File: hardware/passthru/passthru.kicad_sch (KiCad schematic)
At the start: 81 parts, among them J1 ARM_SWD, J2 RJ45_LED_Shielded, J3 Screw_Terminal_01x02, Q1 Q_PMOS_DGS, Q2 Q_PMOS_DGS, Q3 Q_NPN_BEC, U1 EFM32GG11B8xx, U2 KSZ8081RND, U3 LM5085, U4 TPS2375-1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

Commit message: passthru: change package for C28
This is a larger-capacity capacitor.
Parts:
- C28: footprint Capacitor_SMD:C_0603_1608Metric_Pad1.08x0.95mm_HandSolder -> Capacitor_SMD:CP_Elec_6.3x5.8
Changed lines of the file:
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@@
       (effects (font (size 1.27 1.27)) (justify left))
     )
-    (property "Footprint" "Capacitor_SMD:C_0603_1608Metric_Pad1.08x0.95mm_HandSolder" (id 2) (at 260.35 152.4 0)
+    (property "Footprint" "Capacitor_SMD:CP_Elec_6.3x5.8" (id 2) (at 260.35 152.4 0)
       (effects (font (size 1.27 1.27)) hide)
     )
@@
     )
     (path "/3e114920-c983-47e2-a4af-ffa9d93bf066"
-      (reference "C28") (unit 1) (value "100u") (footprint "Capacitor_SMD:C_0603_1608Metric_Pad1.08x0.95mm_HandSolder")
+      (reference "C28") (unit 1) (value "100u") (footprint "Capacitor_SMD:CP_Elec_6.3x5.8")
     )
     (path "/705e5d5e-846d-457e-8c79-943d88941cdd"

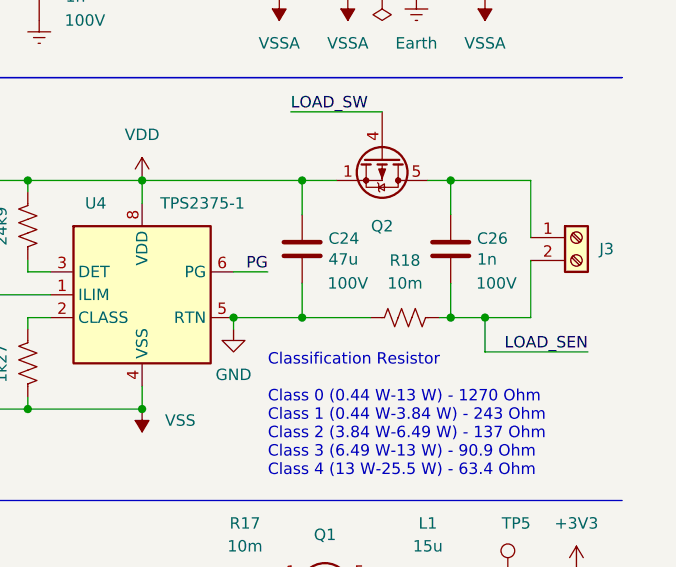
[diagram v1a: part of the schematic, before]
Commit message: passthru: increase the resistance of the VDD shunt resistor
Assuming a maximum VDD current of 600 mA, this will give a maximum
sense voltage of 0.6 V and 36 mW of power draw.
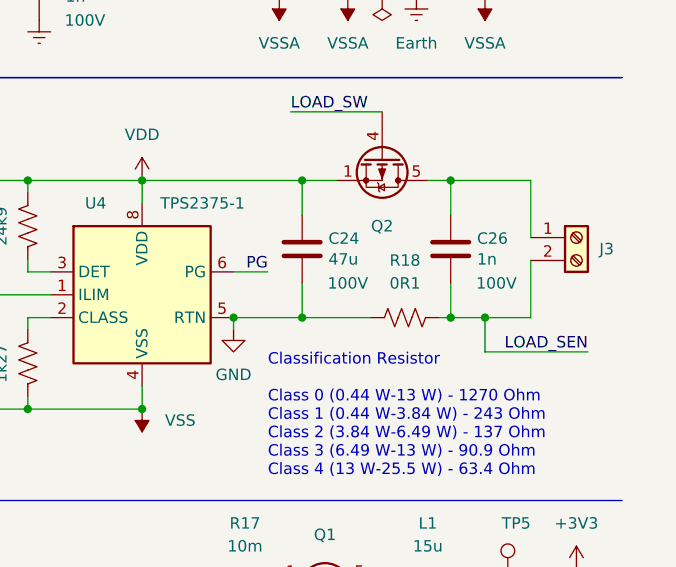
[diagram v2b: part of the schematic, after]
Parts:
- R18: value 10m -> 0R1
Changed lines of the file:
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@@
     (in_bom yes) (on_board yes) (fields_autoplaced)
     (property "Reference" "R18" (id 0) (at 241.3 104.14 90))
-    (property "Value" "10m" (id 1) (at 241.3 106.68 90))
+    (property "Value" "0R1" (id 1) (at 241.3 106.68 90))
     (property "Footprint" "Resistor_SMD:R_0805_2012Metric_Pad1.20x1.40mm_HandSolder" (id 2) (at 241.554 109.474 90)
       (effects (font (size 1.27 1.27)) hide)
@@
     )
     (path "/2fbf6397-d758-4da9-b1f6-76896aa5eb14"
-      (reference "R18") (unit 1) (value "10m") (footprint "Resistor_SMD:R_0805_2012Metric_Pad1.20x1.40mm_HandSolder")
+      (reference "R18") (unit 1) (value "0R1") (footprint "Resistor_SMD:R_0805_2012Metric_Pad1.20x1.40mm_HandSolder")
     )
     (path "/49b4fa8c-c9be-4919-acc5-cb23c2bb3e6c"

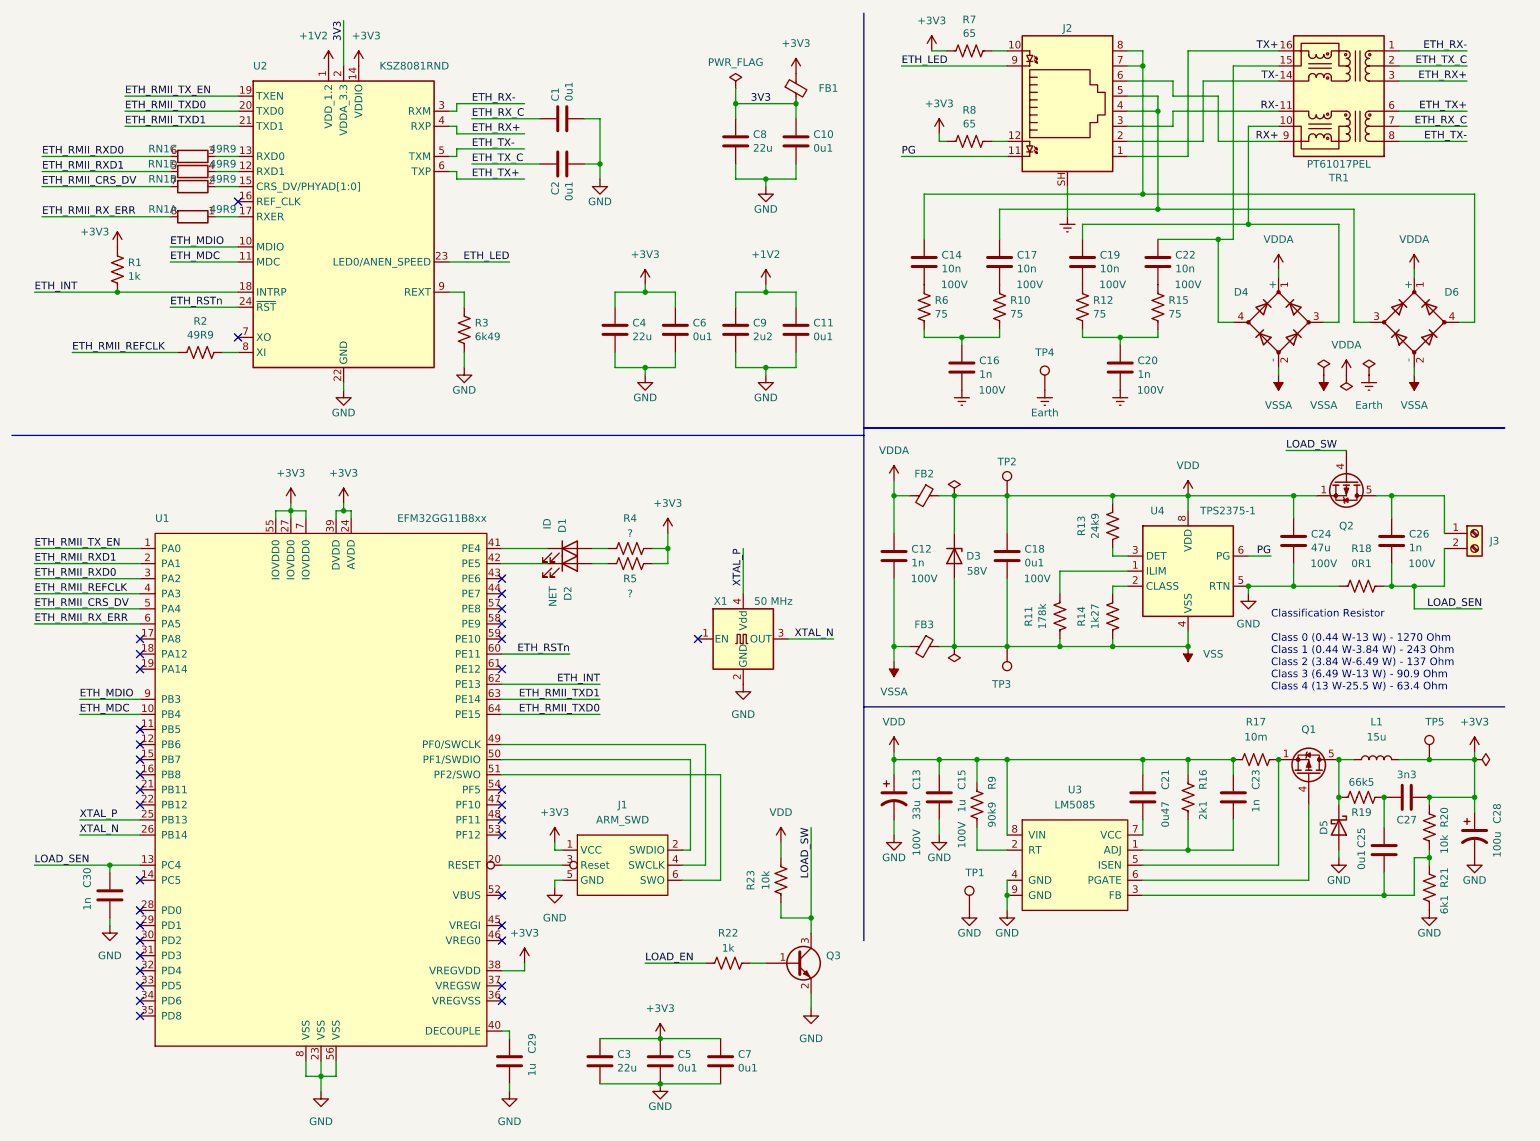
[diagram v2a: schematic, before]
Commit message: passthru: update resistor values
The 6.1 kΩ resistor was hard to find. I also added the
current-limiting resistors for the LEDs.
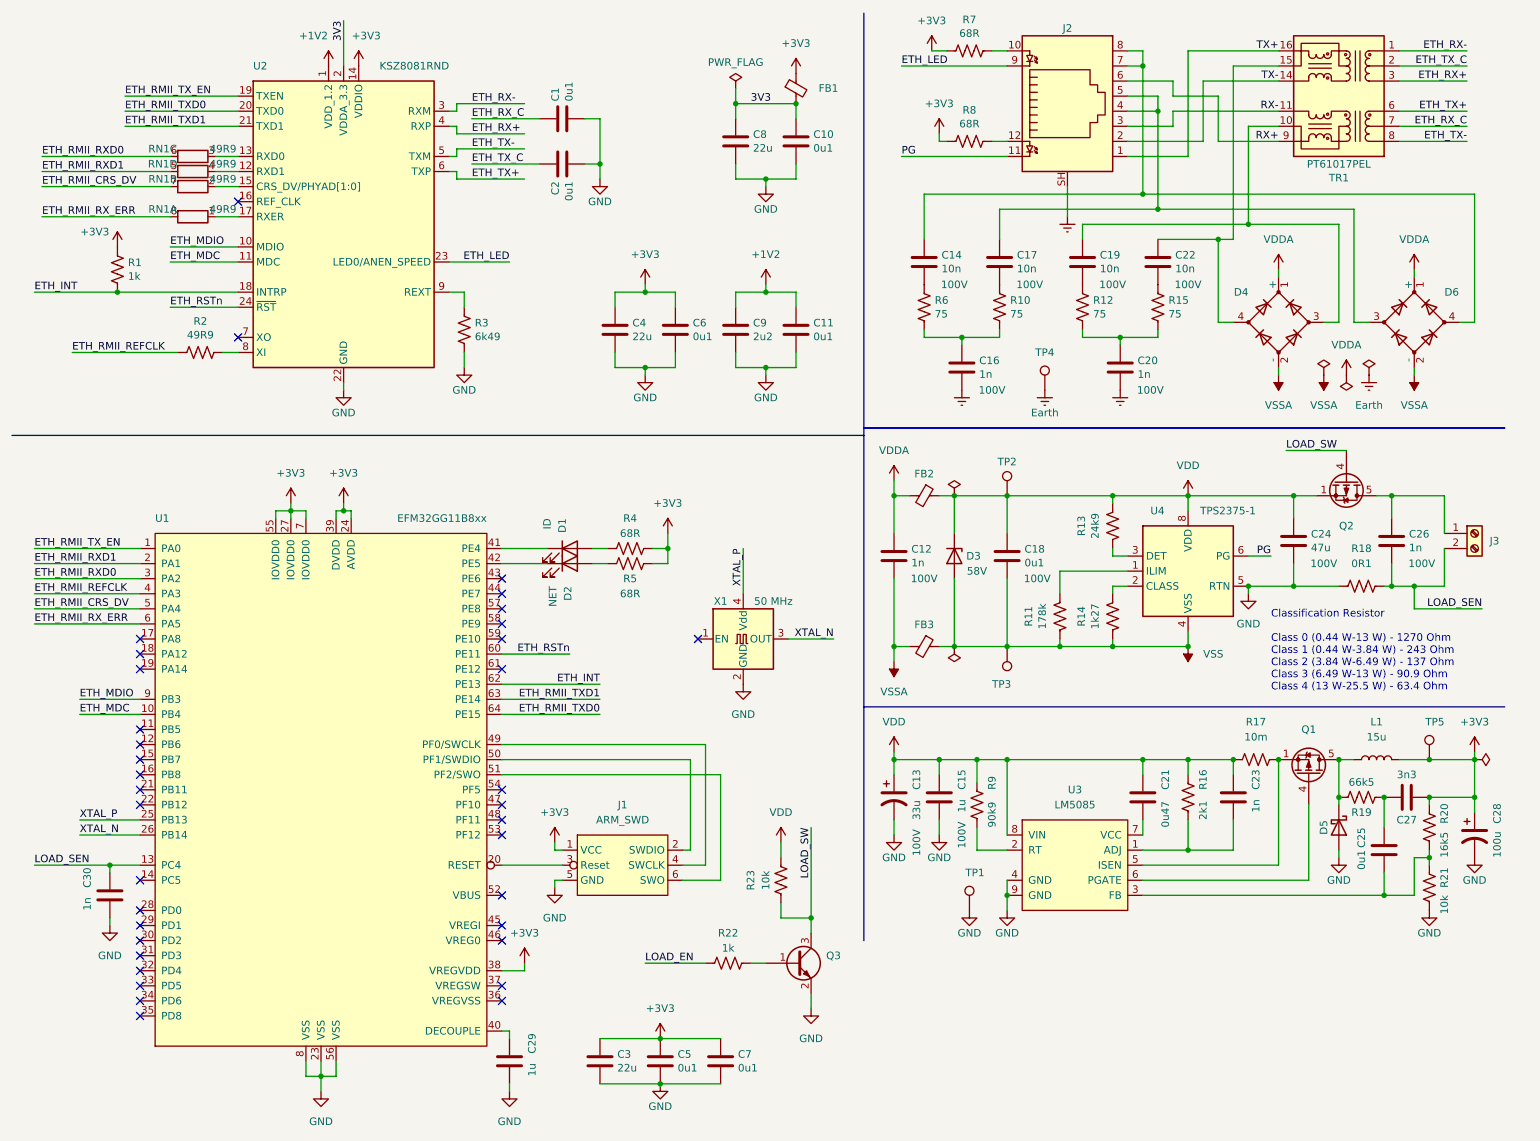
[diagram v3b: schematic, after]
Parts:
- R20: value 10k -> 16k5
- R21: value 6k1 -> 10k
- R4, R5: value ? -> 68R
- R7, R8: value 65 -> 68R; footprint Capacitor_SMD:C_0603_1608Metric_Pad1.08x0.95mm_HandSolder -> Resistor_SMD:R_0603_1608Metric_Pad0.98x0.95mm_HandSolder
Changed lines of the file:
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@@
   (symbol (lib_id "Device:R_US") (at 252.73 151.13 0) (unit 1)
     (in_bom yes) (on_board yes)
-    (property "Reference" "R20" (id 0) (at 255.27 151.13 90)
-      (effects (font (size 1.27 1.27)) (justify left))
-    )
-    (property "Value" "10k" (id 1) (at 255.27 155.575 90)
+    (property "Reference" "R20" (id 0) (at 255.27 150.495 90)
+      (effects (font (size 1.27 1.27)) (justify left))
+    )
+    (property "Value" "16k5" (id 1) (at 255.27 156.21 90)
       (effects (font (size 1.27 1.27)) (justify left))
     )
@@
     (in_bom yes) (on_board yes)
     (property "Reference" "R8" (id 0) (at 175.26 30.3022 90))
-    (property "Value" "65" (id 1) (at 175.26 32.6136 90))
-    (property "Footprint" "Capacitor_SMD:C_0603_1608Metric_Pad1.08x0.95mm_HandSolder" (id 2) (at 175.006 36.576 90)
+    (property "Value" "68R" (id 1) (at 175.26 32.6136 90))
+    (property "Footprint" "Resistor_SMD:R_0603_1608Metric_Pad0.98x0.95mm_HandSolder" (id 2) (at 175.006 36.576 90)
       (effects (font (size 1.27 1.27)) hide)
     )
@@
     (in_bom yes) (on_board yes)
     (property "Reference" "R7" (id 0) (at 175.26 15.0622 90))
-    (property "Value" "65" (id 1) (at 175.26 17.3736 90))
-    (property "Footprint" "Capacitor_SMD:C_0603_1608Metric_Pad1.08x0.95mm_HandSolder" (id 2) (at 175.006 21.336 90)
+    (property "Value" "68R" (id 1) (at 175.26 17.3736 90))
+    (property "Footprint" "Resistor_SMD:R_0603_1608Metric_Pad0.98x0.95mm_HandSolder" (id 2) (at 175.006 21.336 90)
       (effects (font (size 1.27 1.27)) hide)
     )
@@
     (in_bom yes) (on_board yes)
     (property "Reference" "R5" (id 0) (at 118.11 109.22 90))
-    (property "Value" "?" (id 1) (at 118.11 111.76 90))
+    (property "Value" "68R" (id 1) (at 118.11 111.76 90))
     (property "Footprint" "Resistor_SMD:R_0603_1608Metric_Pad0.98x0.95mm_HandSolder" (id 2) (at 118.364 105.664 90)
       (effects (font (size 1.27 1.27)) hide)
@@
     (in_bom yes) (on_board yes)
     (property "Reference" "R4" (id 0) (at 118.11 99.06 90))
-    (property "Value" "?" (id 1) (at 118.11 101.6 90))
+    (property "Value" "68R" (id 1) (at 118.11 101.6 90))
     (property "Footprint" "Resistor_SMD:R_0603_1608Metric_Pad0.98x0.95mm_HandSolder" (id 2) (at 118.364 103.124 90)
       (effects (font (size 1.27 1.27)) hide)
@@
       (effects (font (size 1.27 1.27)) (justify left))
     )
-    (property "Value" "6k1" (id 1) (at 255.27 165.735 90)
+    (property "Value" "10k" (id 1) (at 255.27 165.735 90)
       (effects (font (size 1.27 1.27)) (justify left))
     )
@@
     )
     (path "/a704724f-4b2e-47f2-9716-1986d43798c2"
-      (reference "R4") (unit 1) (value "?") (footprint "Resistor_SMD:R_0603_1608Metric_Pad0.98x0.95mm_HandSolder")
+      (reference "R4") (unit 1) (value "68R") (footprint "Resistor_SMD:R_0603_1608Metric_Pad0.98x0.95mm_HandSolder")
     )
     (path "/9d4e9158-a79b-4cd2-a875-493d31ceebff"
-      (reference "R5") (unit 1) (value "?") (footprint "Resistor_SMD:R_0603_1608Metric_Pad0.98x0.95mm_HandSolder")
+      (reference "R5") (unit 1) (value "68R") (footprint "Resistor_SMD:R_0603_1608Metric_Pad0.98x0.95mm_HandSolder")
     )
     (path "/2e130a9d-a852-4c24-b5aa-0bcd4d7d6efc"
@@
     )
     (path "/8215b5c3-e92a-447c-93b6-8f77bba9d70d"
-      (reference "R7") (unit 1) (value "65") (footprint "Capacitor_SMD:C_0603_1608Metric_Pad1.08x0.95mm_HandSolder")
+      (reference "R7") (unit 1) (value "68R") (footprint "Resistor_SMD:R_0603_1608Metric_Pad0.98x0.95mm_HandSolder")
     )
     (path "/7defcb95-dc82-483d-8346-733eed4831e7"
-      (reference "R8") (unit 1) (value "65") (footprint "Capacitor_SMD:C_0603_1608Metric_Pad1.08x0.95mm_HandSolder")
+      (reference "R8") (unit 1) (value "68R") (footprint "Resistor_SMD:R_0603_1608Metric_Pad0.98x0.95mm_HandSolder")
     )
     (path "/c54f8170-45ef-4d10-a60a-edfecf86c5a3"
@@
     )
     (path "/6a2fc3c1-7ad8-4e78-a7bf-386619f2ac37"
-      (reference "R20") (unit 1) (value "10k") (footprint "Resistor_SMD:R_0603_1608Metric_Pad0.98x0.95mm_HandSolder")
+      (reference "R20") (unit 1) (value "16k5") (footprint "Resistor_SMD:R_0603_1608Metric_Pad0.98x0.95mm_HandSolder")
     )
     (path "/b0467ca9-1c9f-4a10-b539-7dd819231f4d"
-      (reference "R21") (unit 1) (value "6k1") (footprint "Resistor_SMD:R_0603_1608Metric_Pad0.98x0.95mm_HandSolder")
+      (reference "R21") (unit 1) (value "10k") (footprint "Resistor_SMD:R_0603_1608Metric_Pad0.98x0.95mm_HandSolder")
     )
     (path "/853b7b04-0b27-4810-8c5b-d307f69676d7"

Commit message: passthru: update footprint for C24
This needs to be larger because of the higher voltage.
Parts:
- C24: footprint Capacitor_SMD:C_0603_1608Metric_Pad1.08x0.95mm_HandSolder -> Capacitor_SMD:CP_Elec_10x12.5
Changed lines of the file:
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@@
       (effects (font (size 1.27 1.27)) (justify left))
     )
-    (property "Footprint" "Capacitor_SMD:C_0603_1608Metric_Pad1.08x0.95mm_HandSolder" (id 2) (at 230.8352 106.68 0)
+    (property "Footprint" "Capacitor_SMD:CP_Elec_10x12.5" (id 2) (at 230.8352 106.68 0)
       (effects (font (size 1.27 1.27)) hide)
     )
@@
     )
     (path "/45a9e99b-2ed2-4428-aa5d-cf584bf9b8b4"
-      (reference "C24") (unit 1) (value "47u") (footprint "Capacitor_SMD:C_0603_1608Metric_Pad1.08x0.95mm_HandSolder")
+      (reference "C24") (unit 1) (value "47u") (footprint "Capacitor_SMD:CP_Elec_10x12.5")
     )
     (path "/3aef0b22-bfe1-40c2-a910-0405ad1cb17f"
